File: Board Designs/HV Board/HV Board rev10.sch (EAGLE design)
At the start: 62 parts, among them IC1 OKI-78SR-5, IC2 NE5532SOIC

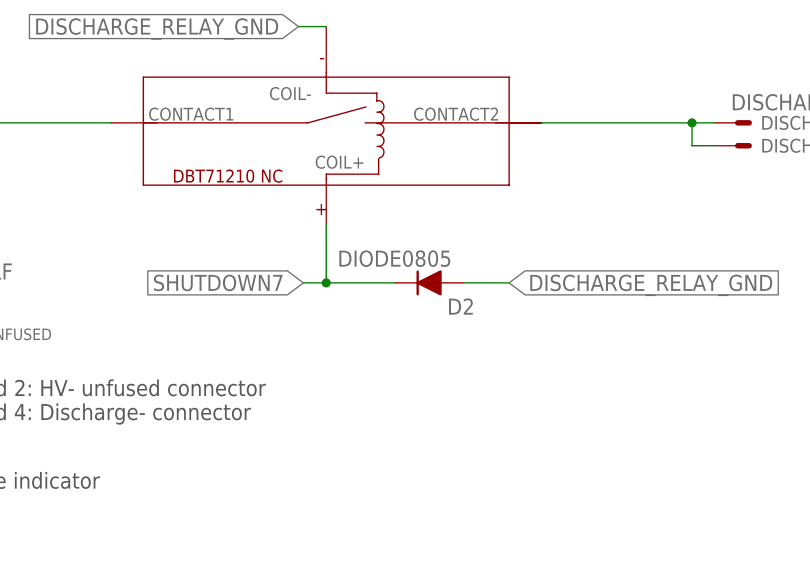
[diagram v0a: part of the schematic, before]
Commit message: HV board rev10: moved LTC6820 and screw
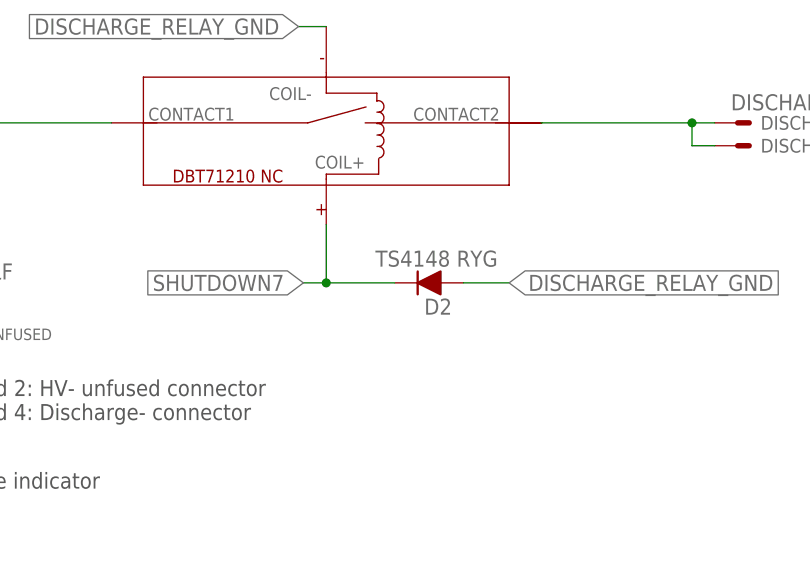
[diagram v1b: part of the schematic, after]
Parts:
- D2: value DIODE0805 -> TS4148 RYG
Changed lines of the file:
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@@
 <part name="D1" library="HyTechDevices" deviceset="DIODE" device="DO-41" value="DIODE"/>
 <part name="C1" library="HyTechDevices" deviceset="CAP" device="" value="180µF"/>
-<part name="D2" library="HyTechDevices" deviceset="DIODE" device="0805"/>
 <part name="R27" library="HyTechDevices" deviceset="RESISTOR" device="0805-RES" value="120"/>
 <part name="GND13" library="HyTech 2016" deviceset="GND" device=""/>
@@
 <part name="R7" library="HyTechDevices" deviceset="RESISTOR" device="0805-RES" value="12k"/>
 <part name="GND20" library="supply1" deviceset="GND" device=""/>
+<part name="D2" library="HyTechDevices" deviceset="DIODE" device="0805" value="TS4148 RYG"/>
 </parts>
 <sheets>
@@
 <attribute name="VALUE" x="225.044" y="-78.359" size="1.778" layer="96"/>
 </instance>
-<instance part="D2" gate="1" x="276.86" y="-78.74" smashed="yes" rot="R180">
-<attribute name="NAME" x="283.21" y="-80.4926" size="1.778" layer="95" rot="R180"/>
-<attribute name="VALUE" x="280.67" y="-75.1586" size="1.778" layer="96" rot="R180"/>
-</instance>
 <instance part="R27" gate="G$1" x="25.4" y="-228.6" smashed="yes" rot="MR90">
 <attribute name="NAME" x="26.8986" y="-232.41" size="1.778" layer="95" rot="MR90"/>
@@
 <instance part="GND20" gate="1" x="38.1" y="-99.06" smashed="yes" rot="R270">
 <attribute name="VALUE" x="35.56" y="-96.52" size="1.778" layer="96" rot="R270"/>
+</instance>
+<instance part="D2" gate="1" x="276.86" y="-78.74" smashed="yes" rot="R180">
+<attribute name="NAME" x="280.67" y="-80.4926" size="1.778" layer="95" rot="R180"/>
+<attribute name="VALUE" x="285.75" y="-75.1586" size="1.778" layer="96" rot="R180"/>
 </instance>
 </instances>
@@
 <net name="SHUTDOWN7" class="0">
 <segment>
-<pinref part="D2" gate="1" pin="C"/>
 <wire x1="266.7" y1="-78.74" x2="266.7" y2="-72.26" width="0.1524" layer="91"/>
-<wire x1="274.32" y1="-78.74" x2="266.7" y2="-78.74" width="0.1524" layer="91"/>
 <label x="264.16" y="-78.74" size="1.778" layer="95" rot="R180" xref="yes"/>
 <wire x1="266.7" y1="-78.74" x2="264.16" y2="-78.74" width="0.1524" layer="91"/>
+<pinref part="U$4" gate="G$1" pin="COIL+"/>
+<pinref part="D2" gate="1" pin="C"/>
+<wire x1="274.32" y1="-78.74" x2="266.7" y2="-78.74" width="0.1524" layer="91"/>
 <junction x="266.7" y="-78.74"/>
-<pinref part="U$4" gate="G$1" pin="COIL+"/>
 </segment>
 <segment>
@@
 <net name="DISCHARGE_RELAY_GND" class="0">
 <segment>
-<pinref part="D2" gate="1" pin="A"/>
 <wire x1="281.94" y1="-78.74" x2="287.02" y2="-78.74" width="0.1524" layer="91"/>
 <label x="287.02" y="-78.74" size="1.778" layer="95" xref="yes"/>
-</segment>
-<segment>
+<pinref part="D2" gate="1" pin="A"/>
+</segment>
+<segment>
